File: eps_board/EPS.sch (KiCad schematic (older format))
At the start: 0 parts

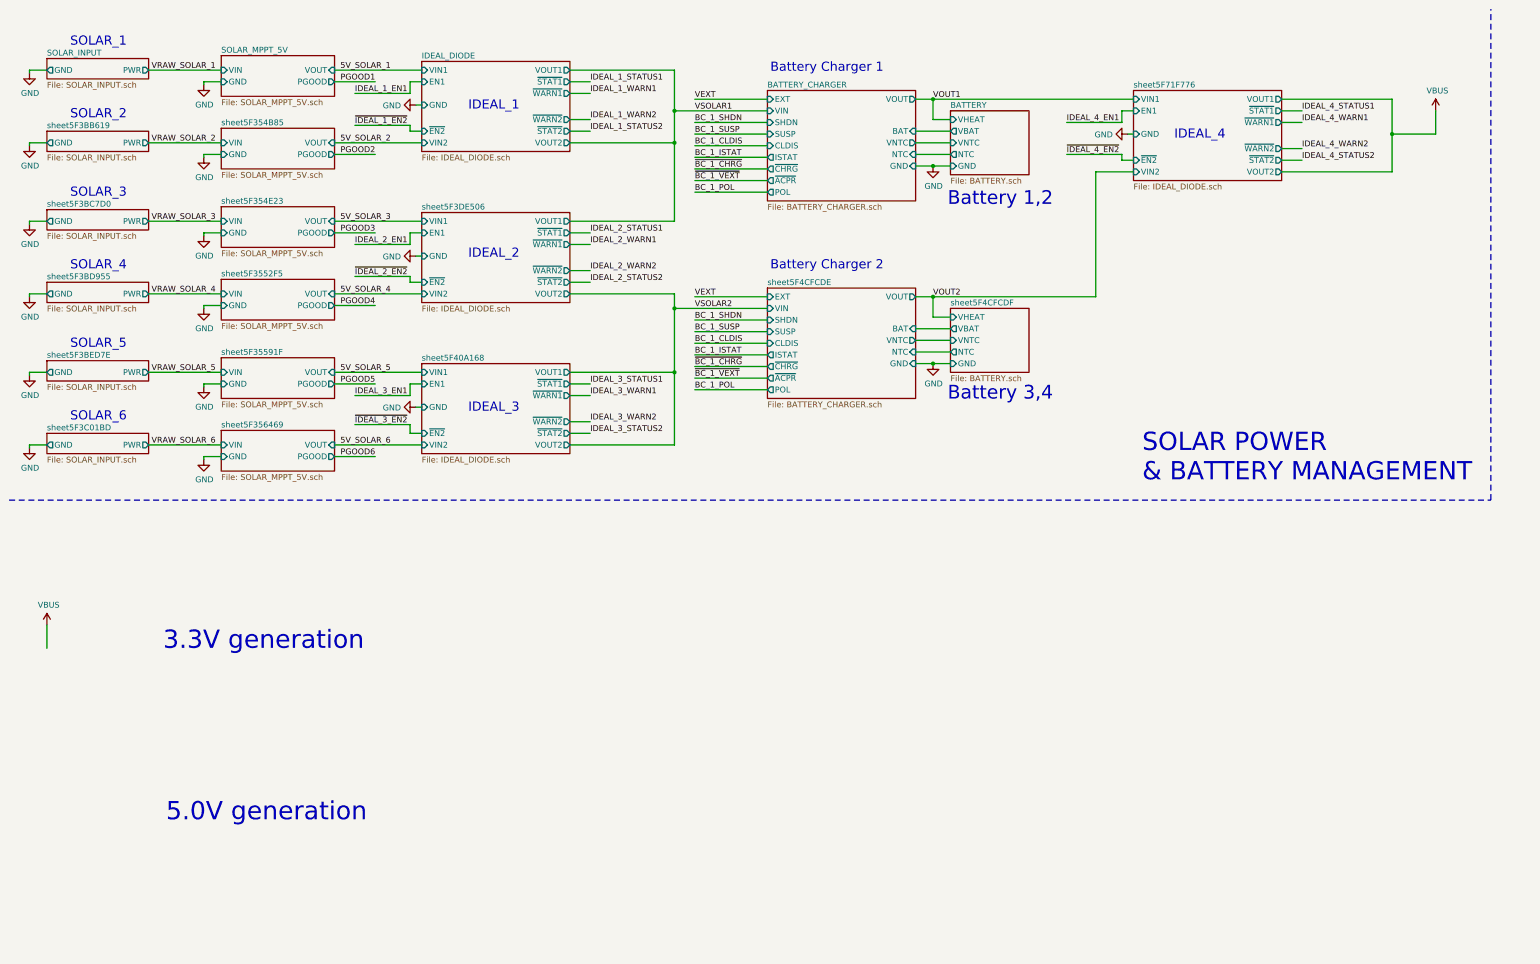
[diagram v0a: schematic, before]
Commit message: EPS with schottky diodes & 1 regulator
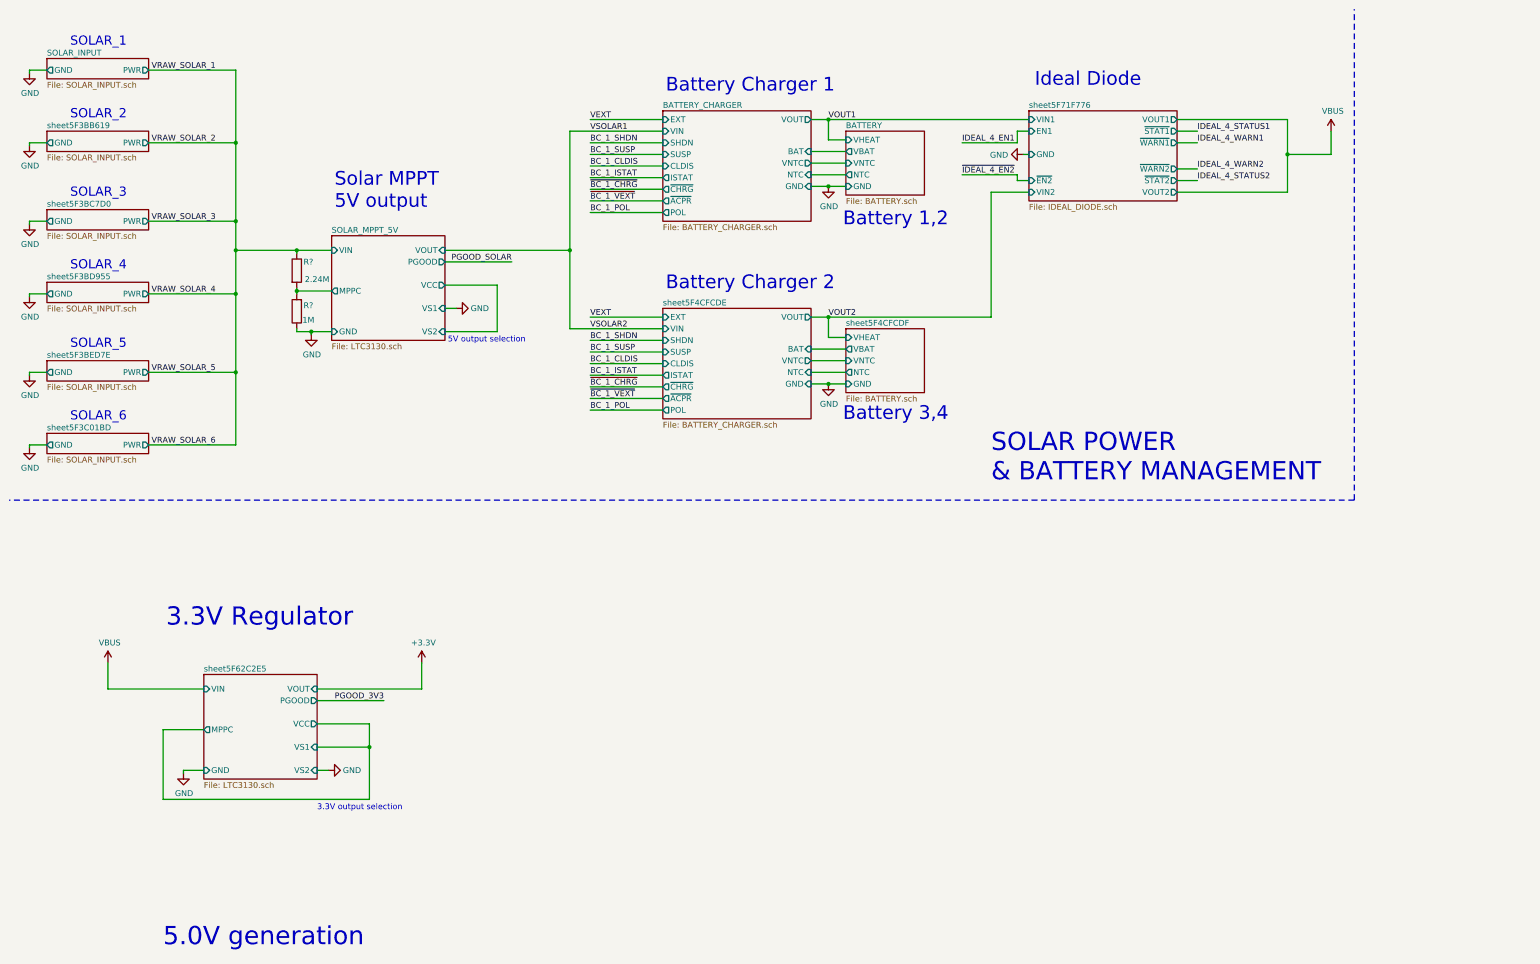
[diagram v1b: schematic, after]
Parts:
- added R?: 1M, Resistor_SMD:R_0603_1608Metric_Pad1.05x0.95mm_HandSolder, symbol Device:R
- added R?: 2.24M, Resistor_SMD:R_0603_1608Metric_Pad1.05x0.95mm_HandSolder, symbol Device:R
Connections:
- net GND: now also R?.1
- net VRAW_SOLAR_1: now also R?.1
- new net SOLAR_MPPT_5V/MPPC: R?.2, R?.2
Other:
- note added: "3.3V Regulator"
- note added: "3.3V output selection"
- note added: "5V output selection"
- note added: "Ideal Diode"
- note added: "Solar MPPT \n5V output"
- note removed: "3.3V generation"
- note removed: "IDEAL_1"
- note removed: "IDEAL_2"
- note removed: "IDEAL_3"
- note removed: "IDEAL_4"

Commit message: Progress on EPS
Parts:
- added C? (x2): 0.1uF, Capacitor_SMD:C_0603_1608Metric_Pad1.05x0.95mm_HandSolder, symbol Device:C
- added R? (x5): 10m, Resistor_SMD:R_0603_1608Metric_Pad1.05x0.95mm_HandSolder, symbol Device:R
- added R? (x15): 100k, Resistor_SMD:R_0603_1608Metric_Pad1.05x0.95mm_HandSolder, symbol Device:R
- added R?: 100K, Resistor_SMD:R_0603_1608Metric_Pad1.05x0.95mm_HandSolder, symbol Device:R
- added R? (x2): 10k, Resistor_SMD:R_0603_1608Metric_Pad1.05x0.95mm_HandSolder, symbol Device:R
- added R? (x2): 0, Resistor_SMD:R_0603_1608Metric_Pad1.05x0.95mm_HandSolder, symbol Device:R_Small
- added R? (x2): 150k, Resistor_SMD:R_0603_1608Metric_Pad1.05x0.95mm_HandSolder, symbol Device:R
- added U? (x2): TPS270, Package_TO_SOT_SMD:TSOT-23-6_HandSoldering, symbol 1K_Custom_Symbol:TPS270
- added U? (x2): 74LVC1G07, Package_TO_SOT_SMD:SOT-353_SC-70-5_Handsoldering, symbol 74xGxx:74LVC1G07
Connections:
- net +3V3: now also C?.2, C?.2, U?.2 (VOUT), U?.3 (VOUT), U?.5 (VCC), U?.5 (VCC)
- net BC_1_POL: now also R?.1
- net GND: now also C?.1, C?.1, R?.1, R?.1, R?.1, R?.1, U?.1 (R2), U?.1 (R2), U?.3 (GND), U?.3 (GND)
- net PGOOD_SOLAR: now also R?.1
- net VBUS: now also R?.1, R?.1
- net VOUT1: now also R?.1, R?.2
- net VOUT2: now also R?.1, R?.2
- net ~BC_1_CHRG: now also R?.1
- net VRAW_SOLAR_1 renamed VRAW_SOLAR
- new net: R?.2, U?.2 (VOUT), U?.3 (VOUT)
- new net: R?.1, U?.6 (R1/C1) (x2)
- new net 3.3V_EPS_STM: R?.1, R?.1, R?.1, R?.2, R?.2, R?.2, R?.2, R?.2, R?.2
- new net AVI_EXTRN_RST: R?.2
- new net BC_2_POL: R?.1
- new net CURRENT_MONITORS/RST1_13: U?.4, U?.4
- new net EPS_EXTRN_RST: R?.2, U?.2
- new net EPS_WATCHDOG: U?.2
- new net IDEAL_EN1: R?.1
- new net INTERBOARD_CONNECTOR/AVI_RESET: R?.1
- new net INTERBOARD_CONNECTOR/EPS_RESET: R?.1
- new net PG_3V3: R?.1, U?.5 (EN)
- new net PG_SOLAR: R?.1, U?.5 (EN)
- new net PMIC/ADC1_IN10: R?.2, R?.2
- new net PMIC/ADC1_IN11: R?.2, R?.2
- new net PMIC/ADC1_IN9: R?.2, R?.2
- new net SOLAR_5V: R?.1, R?.1
- new net SOLAR_MPPT_5V/VOUT: R?.2, R?.2, U?.4 (VIN)
- new net sheet5F71F776/VIN1: R?.1
- new net sheet5F71F776/VIN2: R?.1
- new net sheet5F71F776/VOUT1: R?.2
- new net sheet5F71F776/VOUT2: R?.2
- new net sheet5FCD3934/VOUT: R?.2, R?.2, U?.4 (VIN)
- new net ~BC_2_CHRG: R?.1
- new net ~IDEAL_EN2: R?.2
- new net ~IDEAL_STATUS1: R?.2
- new net ~IDEAL_STATUS2: R?.2
- new net ~IDEAL_WARN1: R?.2
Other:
- note added: "2A @ 4Vin Max"
- note added: "3.3V output"
- note added: "300mA Output Max"
- note added: "5.0V Regulator"
- note added: "5V output"
- note added: "Current Monitors &\nLoad switching"
- note added: "EPS Reset Triggers"
- note added: "Interboard Connector"
- note added: "OUT=0.5*IN"
- note added: "OUT=0.6*IN"
- note added: "Power Good\nLoad Switch"
- note added: "Power Management IC (PMIC)"
- note added: "Roughly 150mA from one solar panel \nunder good conditions. \nMAYBE 200mA with multiple sides"
- note added: "Voltage Regulators"
- note removed: "3.3V output selection"
- note removed: "5.0V generation"
- note removed: "5V output selection"
- moved on the sheet: R?

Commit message: Essentially done with EPS schematic
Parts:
- added D18: ESD9B5.0ST5G, Diode_SMD:D_SOD-923, symbol Diode:ESD9B5.0ST5G
- added D19: LED_SMD_RED, LED_SMD:LED_0603_1608Metric_Pad1.05x0.95mm_HandSolder, symbol Device:LED_Small_ALT
- added J14: USB_B_Micro, Connector_USB:USB_Micro-B_Amphenol_10103594-0001LF_Horizontal, symbol Connector:USB_B_Micro
- added R327: 0, Resistor_SMD:R_0603_1608Metric_Pad1.05x0.95mm_HandSolder, symbol Device:R
- added R328: 10m, Resistor_SMD:R_0603_1608Metric_Pad1.05x0.95mm_HandSolder, symbol Device:R
- added R329: 330, Resistor_SMD:R_0603_1608Metric_Pad1.05x0.95mm_HandSolder, symbol Device:R
- C19, C20: renamed from C?; Mfr. # (none) -> CL10B104KA8NNNC; Order (none) -> https://www.digikey.com/product-detail/en/samsung-electro-m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; Voltage (none) -> 25V
- R10: renamed from R?; value 1M -> 100K; Mfr. # (none) -> RMCF0603FT100K; Order (none) -> https://www.digikey.com/en/products/detail/stackpole-electr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
- R11, R48: renamed from R?; value 10k -> 10K; Mfr. # (none) -> RMCF0603FT10K0; Order (none) -> https://www.digikey.com/en/products/detail/stackpole-electr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
- R12, R16, R17, R18, R32, R33, R42, R44, R45, R46, R47, R50, R51, R52, R8: renamed from R?; value 100k -> 100K; Mfr. # (none) -> RMCF0603FT100K; Order (none) -> https://www.digikey.com/en/products/detail/stackpole-electr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
- R13: renamed from R?; Mfr. # (none) -> RMCF0603FT100K; Order (none) -> https://www.digikey.com/en/products/detail/stackpole-electr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
- R34, R43: renamed from R?; value 150k -> 150K; Mfr. # (none) -> RMCF0603FT150K; Order (none) -> https://www.digikey.com/en/products/detail/stackpole-electr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
- R57, R58: renamed from R?; Mfr. # RK73Z1JTTD -> RK73Z1JTTD; Order https://www.digikey.com/product-detail/en/koa-speer-electronics-inc/RK73Z1JTTD/2019-RK73Z1JTTDCT-ND/9847522 -> https://www.digikey.com/product-detail/en/koa-speer-electronics-inc/RK73Z1JTTD/2019-RK73Z1JTTDCT-ND/9847522
- R9: renamed from R?; value 2.24M -> 224K; Mfr. # (none) -> RMCF0603FT221K; Order (none) -> https://www.digikey.com/en/products/detail/stackpole-electr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
- gave numbers to parts that had none: 9
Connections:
- net GND: now also D18.2 (A2), D19.1 (K), J14.5 (GND), R327.1
- net VEXT: now also D18.1 (A1), R328.1, R329.2
- new net: J14.1 (VBUS), R328.2
- new net: J14.6 (Shield), R327.2
- new net: D19.2 (A), R329.1
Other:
- note added: "Battery 1"
- note added: "Battery 2"
- note added: "External Power"
- note added: "SOLAR POWER &\nBATTERY MANAGEMENT"
- note removed: "Battery 1,2"
- note removed: "Battery 3,4"
- note removed: "SOLAR POWER\n& BATTERY MANAGEMENT"
- moved on the sheet: C19, C20, R11, R12, R13, R16, R17, R18, R32, R33, R34, R42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

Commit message: EPS layout in progress
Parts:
- removed R44, R45: 100K, Resistor_SMD:R_0603_1608Metric_Pad1.05x0.95mm_HandSolder, symbol Device:R
- removed U7: 74LVC1G07, Package_TO_SOT_SMD:SOT-353_SC-70-5_Handsoldering, symbol 74xGxx:74LVC1G07
- added H1: MountingHole, MountingHole:MountingHole_2.1mm, symbol Mechanical:MountingHole
- added H2, H3, H4, H5: MountingHole_Pad, MountingHole:MountingHole_3.2mm_M3_Pad_Via, symbol Mechanical:MountingHole_Pad
- added U7: 74LVC1G07, Package_TO_SOT_SMD:SOT-353_SC-70-5_Handsoldering, symbol 1K_Custom_Symbol:74LVC1G07
- U6: symbol 74xGxx:74LVC1G07 -> 1K_Custom_Symbol:74LVC1G07
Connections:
- net PGOOD_SOLAR is gone; now on net PG_SOLAR: R47.1
- net +3V3: now also U7.5
- net CURRENT_MONITORS/RST1_13: now also U7.4
- net EPS_EXTRN_RST: now also U7.2
- net GND: now also H2.1, H3.1, H4.1, H5.1, U7.3
- net VEXT: no longer D18.1 (A1), R329.2
- net at J14.1 (VBUS), R328.2: now also D18.1 (A1), R329.2
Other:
- note removed: "OUT=0.5*IN"
- moved on the sheet: D18, D19, R328, R329, R42, R43

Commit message: EPS V1.0 Complete
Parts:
- added FID4: Fiducial, Calibration_Scale:Gauge_10mm_Type1_SilkScreenTop, symbol Mechanical:Fiducial
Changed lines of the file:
@@
 F30 "UART_B_RTS" O R 14025 8250 50
 F31 "SPARE_5" O R 14025 7750 50
-F32 "SPARE_6" O R 14025 7850 50
 $EndSheet
 $Comp
@@
 Wire Wire Line
 	5825 2950 6075 2950
+$Comp
+L Mechanical:Fiducial FID4
+U 1 1 5FA9C39C
+P 15400 8350
+F 0 "FID4" H 15485 8396 50  0000 L CNN
+F 1 "Fiducial" H 15485 8305 50  0000 L CNN
+F 2 "Calibration_Scale:Gauge_10mm_Type1_SilkScreenTop" H 15400 8350 50  0001 C CNN
+F 3 "~" H 15400 8350 50  0001 C CNN
+	1    15400 8350
+	1    0    0    -1
+$EndComp
 $EndSCHEMATC
